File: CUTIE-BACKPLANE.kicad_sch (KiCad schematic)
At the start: 0 parts

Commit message: final setup for power rails
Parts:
- added J7: USB3_A, symbol Connector:USB3_A
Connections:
- new net GND: J7.10 (SHIELD), J7.4 (GND), J7.7 (DRAIN)
- new net Slot 6/5V0_USB: J7.1 (VBUS)
- new net USB3.D_N: J7.2 (D-)
- new net USB3.D_P: J7.3 (D+)
- new net USB3.RX_N: J7.5 (SSRX-)
- new net USB3.RX_P: J7.6 (SSRX+)
- new net USB3.TX_N: J7.8 (SSTX-)
- new net USB3.TX_P: J7.9 (SSTX+)
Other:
- sheet Slot 6 ports: added 5V0_USB; removed none

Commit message: initialized for 4-card
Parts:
- added R1, R2: 120, Resistor_SMD:R_0603_1608Metric, symbol Device:R_US
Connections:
- net Slot 6/5V0_USB renamed Slot 1/5V0_USB
- new net CAN0.H: R1.1, R2.1
- new net CAN0.L: R1.2, R2.2
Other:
- removed sheet Slot 5
- removed sheet Slot 6
- sheet Slot 1 ports: added 5V0_1, 5V0_2, 5V0_3, 5V0_USB; removed 5V0, SPI1{SPI}, USB3{USB3}
- sheet Slot 2 ports: added CMRF{SPI}, USB3{USB3}; removed none
- sheet Slot 4 ports: added CMRF{SPI}; removed none
- note added: "CITRUS"
- note added: "Power"
- note added: "RF"
- moved on the sheet: J7

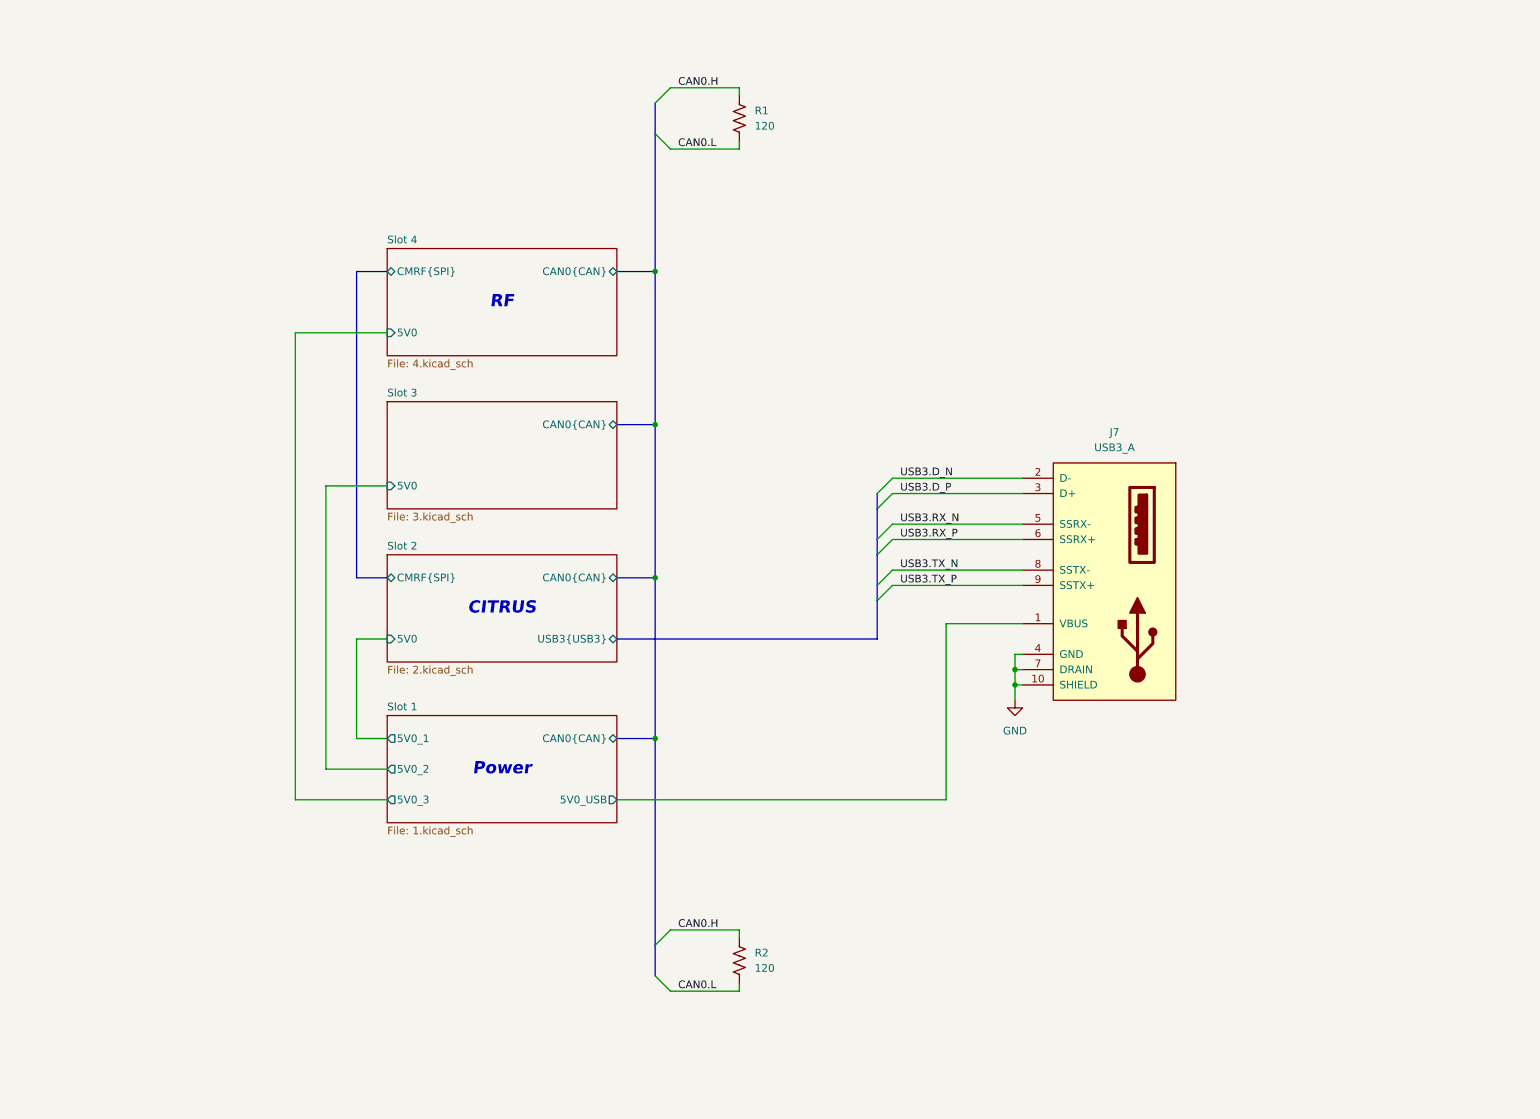
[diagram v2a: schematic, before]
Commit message: added pwr leds and edge cuts
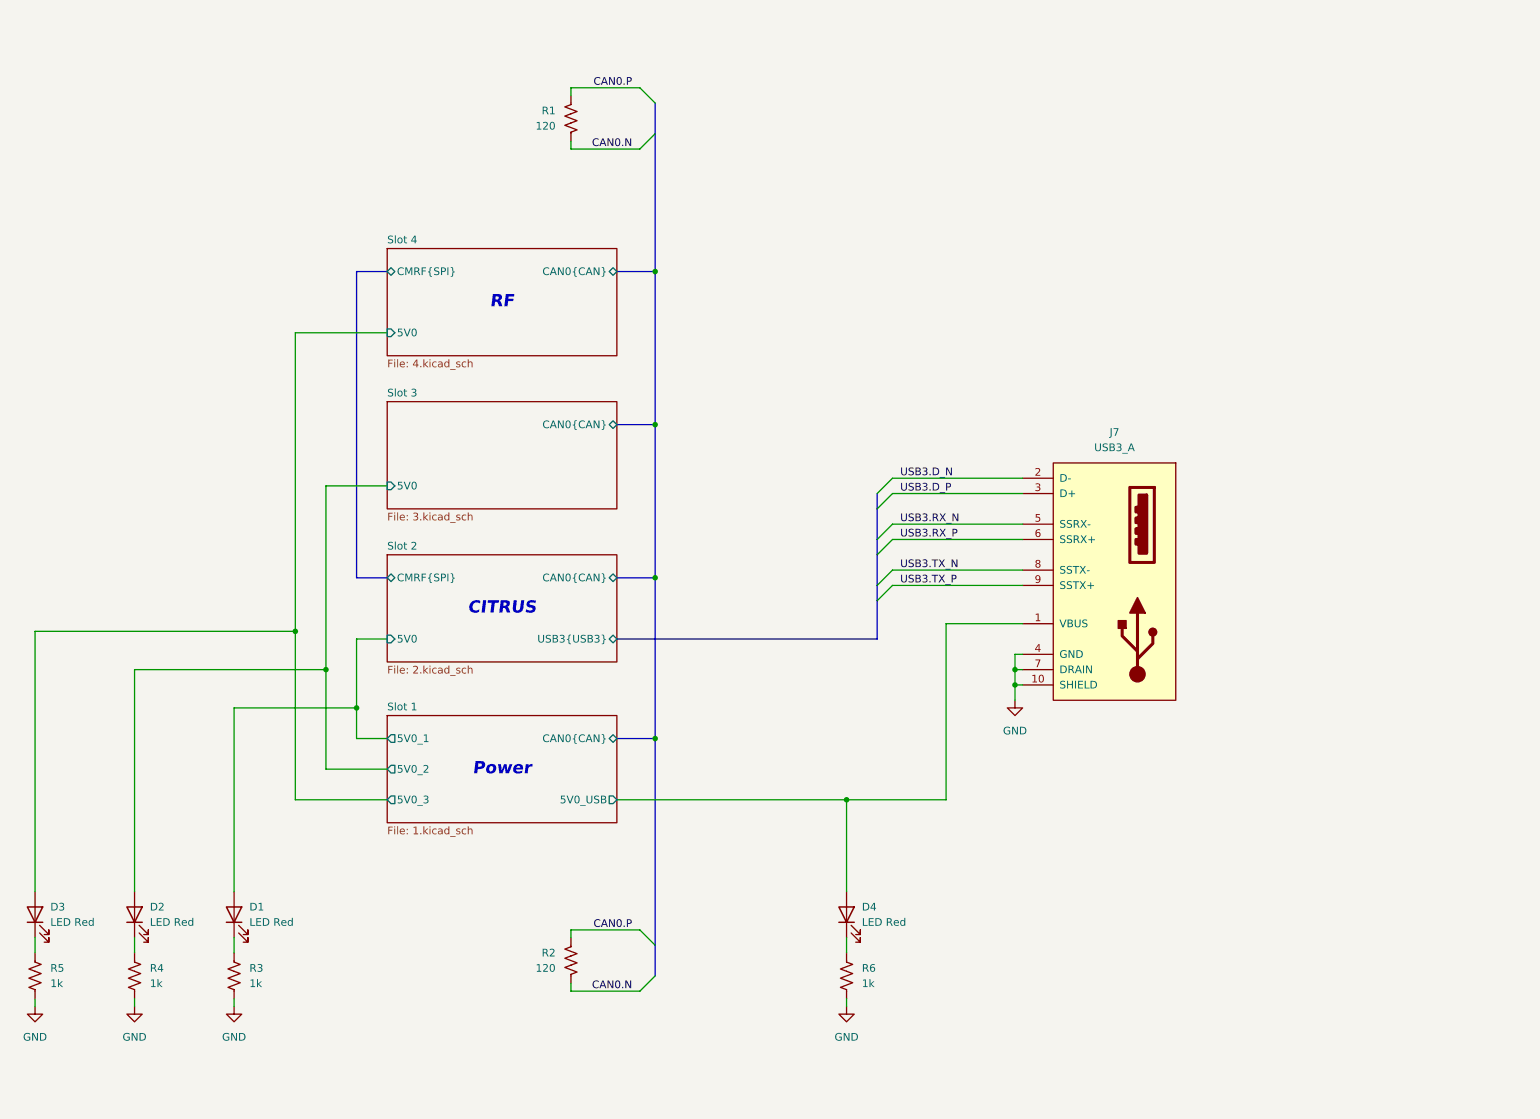
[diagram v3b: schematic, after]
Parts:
- added D1, D2, D3, D4: LED Red, LED_SMD:LED_0603_1608Metric, symbol library:LED
- added R3, R4, R5, R6: 1k, Resistor_SMD:R_0402_1005Metric, symbol library:R_US
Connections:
- net GND: now also R3.2, R4.2, R5.2, R6.2
- net Slot 1/5V0_1: now also D1.2 (A)
- net Slot 1/5V0_2: now also D2.2 (A)
- net Slot 1/5V0_3: now also D3.2 (A)
- net Slot 1/5V0_USB: now also D4.2 (A)
- net CAN0.H renamed CAN0.P
- net CAN0.L renamed CAN0.N
- new net: D4.1 (K), R6.1
- new net: D1.1 (K), R3.1
- new net: D3.1 (K), R5.1
- new net: D2.1 (K), R4.1
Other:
- moved on the sheet: R1, R2

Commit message: prelim layout complete
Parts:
- J7: footprint (none) -> library:CONN9_08-0003_MOL; Manufacturer (none) -> Molex; Manufacturer Product Number (none) -> 0484080003
- R1, R2: Manufacturer (none) -> Vishay Dale; Manufacturer Product Number (none) -> CRCW0402120RFKEDC
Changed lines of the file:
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@@
 			)
 		)
-		(property "Description" ""
+		(property "Description" "RES 1K OHM 5% 1/16W 0402"
 			(at 161.29 175.26 0)
 			(effects
@@
 			)
 		)
-		(property "Description" ""
+		(property "Description" "RES 1K OHM 5% 1/16W 0402"
 			(at 59.69 175.26 0)
 			(effects
@@
 			)
 		)
-		(property "Datasheet" "~"
+		(property "Datasheet" ""
 			(at 115.57 172.72 0)
 			(effects
@@
 			)
 		)
-		(property "Description" "Resistor, US symbol"
+		(property "Description" "RES 120 OHM 1% 1/16W 0402"
 			(at 115.57 172.72 0)
 			(effects
@@
 			)
 		)
+		(property "Manufacturer" "Vishay Dale"
+			(at 115.57 172.72 0)
+			(effects
+				(font
+					(size 1.27 1.27)
+				)
+				(hide yes)
+			)
+		)
+		(property "Manufacturer Product Number" "CRCW0402120RFKEDC"
+			(at 115.57 172.72 0)
+			(effects
+				(font
+					(size 1.27 1.27)
+				)
+				(hide yes)
+			)
+		)
 		(pin "1"
 		)
@@
 				(path "/db751f7b-eeef-4f9a-a021-6b6484a5d83e"
 					(reference "R2")
+					(unit 1)
+				)
+			)
+		)
+	)
+	(symbol
+		(lib_id "Device:R_US")
+		(at 115.57 33.02 0)
+		(mirror y)
+		(unit 1)
+		(exclude_from_sim no)
+		(in_bom yes)
+		(on_board yes)
+		(dnp no)
+		(fields_autoplaced yes)
+		(property "Reference" "R1"
+			(at 113.03 31.7499 0)
+			(effects
+				(font
+					(size 1.27 1.27)
+				)
+				(justify left)
+			)
+		)
+		(property "Value" "120"
+			(at 113.03 34.2899 0)
+			(effects
+				(font
+					(size 1.27 1.27)
+				)
+				(justify left)
+			)
+		)
+		(property "Footprint" "Resistor_SMD:R_0603_1608Metric"
+			(at 114.554 33.274 90)
+			(effects
+				(font
+					(size 1.27 1.27)
+				)
+				(hide yes)
+			)
+		)
+		(property "Datasheet" ""
+			(at 115.57 33.02 0)
+			(effects
+				(font
+					(size 1.27 1.27)
+				)
+				(hide yes)
+			)
+		)
+		(property "Description" "RES 120 OHM 1% 1/16W 0402"
+			(at 115.57 33.02 0)
+			(effects
+				(font
+					(size 1.27 1.27)
+				)
+				(hide yes)
+			)
+		)
+		(property "Manufacturer" "Vishay Dale"
+			(at 115.57 33.02 0)
+			(effects
+				(font
+					(size 1.27 1.27)
+				)
+				(hide yes)
+			)
+		)
+		(property "Manufacturer Product Number" "CRCW0402120RFKEDC"
+			(at 115.57 33.02 0)
+			(effects
+				(font
+					(size 1.27 1.27)
+				)
+				(hide yes)
+			)
+		)
+		(pin "1"
+		)
+		(pin "2"
+		)
+		(instances
+			(project "CUTIE-BACKPLANE"
+				(path "/db751f7b-eeef-4f9a-a021-6b6484a5d83e"
+					(reference "R1")
 					(unit 1)
 				)
@@
 			)
 		)
-		(property "Footprint" ""
+		(property "Footprint" "library:CONN9_08-0003_MOL"
 			(at 201.93 101.6 0)
 			(effects
@@
 			)
 		)
-		(property "Datasheet" "~"
+		(property "Datasheet" ""
 			(at 201.93 101.6 0)
 			(effects
@@
 			)
 		)
-		(property "Description" "USB 3.0 A connector"
+		(property "Description" "CONN RCPT USB3.0 TYPEA 9POS VERT"
 			(at 231.14 128.27 0)
+			(effects
+				(font
+					(size 1.27 1.27)
+				)
+				(hide yes)
+			)
+		)
+		(property "Manufacturer" "Molex"
+			(at 205.74 104.14 0)
+			(effects
+				(font
+					(size 1.27 1.27)
+				)
+				(hide yes)
+			)
+		)
+		(property "Manufacturer Product Number" "0484080003"
+			(at 205.74 104.14 0)
 			(effects
 				(font
@@
 			)
 		)
-		(property "Description" ""
+		(property "Description" "RES 1K OHM 5% 1/16W 0402"
 			(at 26.67 175.26 0)
 			(effects
@@
 	)
 	(symbol
-		(lib_id "Device:R_US")
-		(at 115.57 33.02 0)
-		(mirror y)
-		(unit 1)
-		(exclude_from_sim no)
-		(in_bom yes)
-		(on_board yes)
-		(dnp no)
-		(fields_autoplaced yes)
-		(property "Reference" "R1"
-			(at 113.03 31.7499 0)
-			(effects
-				(font
-					(size 1.27 1.27)
-				)
-				(justify left)
-			)
-		)
-		(property "Value" "120"
-			(at 113.03 34.2899 0)
-			(effects
-				(font
-					(size 1.27 1.27)
-				)
-				(justify left)
-			)
-		)
-		(property "Footprint" "Resistor_SMD:R_0603_1608Metric"
-			(at 114.554 33.274 90)
-			(effects
-				(font
-					(size 1.27 1.27)
-				)
-				(hide yes)
-			)
-		)
-		(property "Datasheet" "~"
-			(at 115.57 33.02 0)
-			(effects
-				(font
-					(size 1.27 1.27)
-				)
-				(hide yes)
-			)
-		)
-		(property "Description" "Resistor, US symbol"
-			(at 115.57 33.02 0)
-			(effects
-				(font
-					(size 1.27 1.27)
-				)
-				(hide yes)
-			)
-		)
-		(pin "1"
-		)
-		(pin "2"
-		)
-		(instances
-			(project ""
-				(path "/db751f7b-eeef-4f9a-a021-6b6484a5d83e"
-					(reference "R1")
-					(unit 1)
-				)
-			)
-		)
-	)
-	(symbol
 		(lib_id "library:R_US")
 		(at 43.18 175.26 0)
@@
 			)
 		)
-		(property "Description" ""
+		(property "Description" "RES 1K OHM 5% 1/16W 0402"
 			(at 43.18 175.26 0)
 			(effects

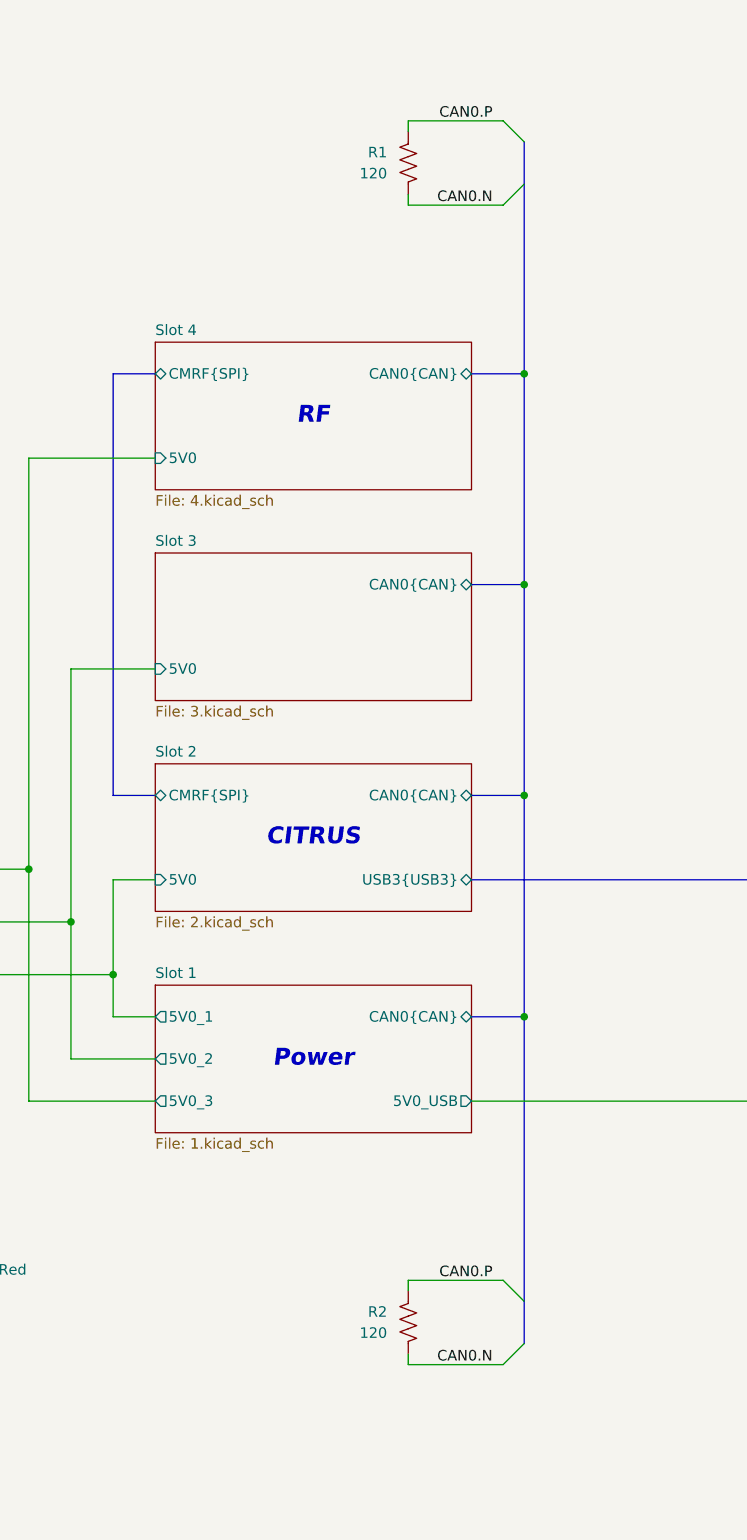
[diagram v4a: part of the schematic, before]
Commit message: added dnps for can filtering
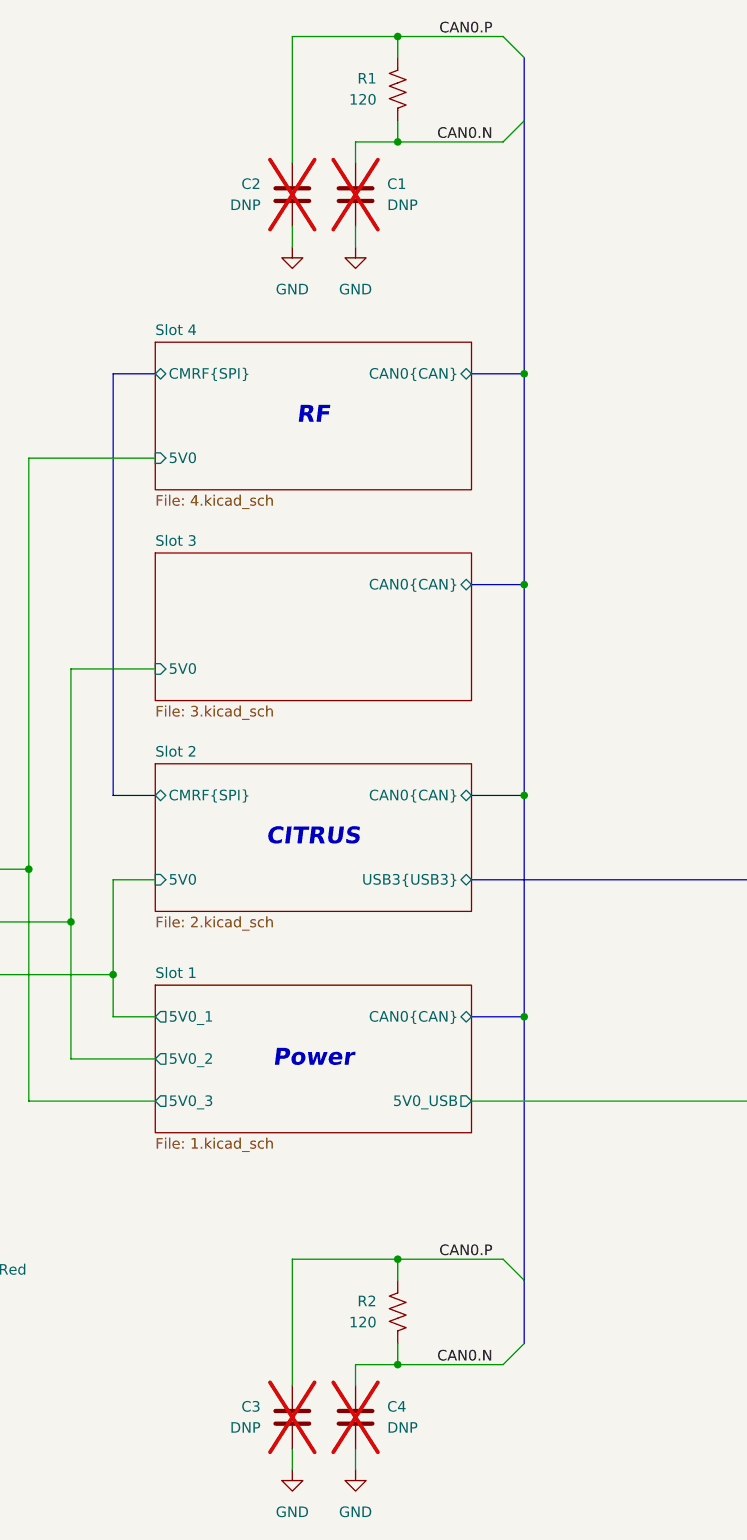
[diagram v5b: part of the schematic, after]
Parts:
- added C1, C2, C3, C4: DNP, Capacitor_SMD:C_0402_1005Metric, symbol Device:C
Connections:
- net CAN0.N: now also C1.2, C4.2
- net CAN0.P: now also C2.2, C3.2
- net GND: now also C1.1, C2.1, C3.1, C4.1
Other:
- moved on the sheet: R1, R2

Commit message: added tps and new init layout
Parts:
- removed D4: LED Red, LED_SMD:LED_0603_1608Metric, symbol library:LED
- removed J7: USB3_A, library:CONN9_08-0003_MOL, symbol Connector:USB3_A
- removed R6: 1k, Resistor_SMD:R_0402_1005Metric, symbol library:R_US
- added J1: USB3_A, library:CONN9_08-0003_MOL, symbol Connector:USB3_A
- R3: renamed from R5; value 1k -> 330
- R4: value 1k -> 330
- R5: renamed from R3; value 1k -> 330
- renumbered D3 to D1, D1 to D3
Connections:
- net CAN0.N: now also C2.2; no longer C1.2
- net CAN0.P: now also C1.2; no longer C2.2
- net GND: now also J1.10 (SHIELD), J1.4 (GND), J1.7 (DRAIN)
- net USB3.D_N: now also J1.2 (D-)
- net USB3.D_P: now also J1.3 (D+)
- net USB3.RX_N: now also J1.5 (SSRX-)
- net USB3.RX_P: now also J1.6 (SSRX+)
- net USB3.TX_N: now also J1.8 (SSTX-)
- net USB3.TX_P: now also J1.9 (SSTX+)
- net LEMON/5V0_1 renamed CITRUS/5V0
- net LEMON/5V0_2 renamed LEMON/5VBUS2
- net LEMON/5VBUS2: now also J1.1 (VBUS)
- net LEMON/5V0_3 renamed LEMON/5VBUS3
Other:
- sheet Slot 1 renamed LEMON
- sheet Slot 2 renamed CITRUS
- sheet Slot 4 renamed ZEST
- removed sheet Slot 3
- sheet CITRUS: file 2.kicad_sch -> sch/citrus.kicad_sch
- sheet LEMON: file 1.kicad_sch -> sch/lemon.kicad_sch
- sheet LEMON ports: added 5VBUS1, 5VBUS2, 5VBUS3; removed 5V0_1, 5V0_2, 5V0_3, 5V0_USB
- sheet ZEST: file 4.kicad_sch -> sch/zest.kicad_sch
- note added: "LEMON"
- note added: "ZEST"
- note removed: "Power"
- note removed: "RF"
- moved on the sheet: D1, D2, D3, R3, R4, R5
